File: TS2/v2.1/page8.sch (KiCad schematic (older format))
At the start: 9 parts, among them SW4 ABORT, U28 74LS148, U32 74LS138, U33 74LS138, U34 74LS00, U35 74LS74, U4 74LS06, U7 74LS08

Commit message: Rev 2.1 design changes.
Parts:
- added unit 4 of U34
- added U37: 74LS00, symbol 74LS00
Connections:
- net GND: now also U34.7 (GND), U37.7 (GND)
- net VCC: now also U34.14 (VCC), U37.14 (VCC)
- net at U4.13: now also U34.11; no longer U34.8
- new net: U34.8, U37.10, U37.9
- new net: U34.12, U37.8
- new net PERI_VPA*: U34.13
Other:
- moved on the sheet: U4F
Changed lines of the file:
@@
 Sheet 9 9
 Title "TS2 68000 Single Board Computer"
-Date "2017-02-14"
+Date "2017-02-15"
 Rev "2.1"
 Comp "Jeff Tranter"
@@
 NoConn ~ 2750 2300
 $Comp
-L VCC #PWR0106
+L VCC #PWR0110
 U 1 1 584DE8AD
 P 3550 1550
-F 0 "#PWR0106" H 3550 1400 50  0001 C CNN
+F 0 "#PWR0110" H 3550 1400 50  0001 C CNN
 F 1 "VCC" H 3550 1700 50  0000 C CNN
 F 2 "" H 3550 1550 50  0000 C CNN
@@
 $EndComp
 $Comp
-L GND #PWR0107
+L GND #PWR0111
 U 1 1 584DE8EB
 P 3550 2450
-F 0 "#PWR0107" H 3550 2200 50  0001 C CNN
+F 0 "#PWR0111" H 3550 2200 50  0001 C CNN
 F 1 "GND" H 3550 2300 50  0000 C CNN
 F 2 "" H 3550 2450 50  0000 C CNN
@@
 FC2
 $Comp
-L VCC #PWR0108
+L VCC #PWR0112
 U 1 1 584E001A
 P 2650 4200
-F 0 "#PWR0108" H 2650 4050 50  0001 C CNN
+F 0 "#PWR0112" H 2650 4050 50  0001 C CNN
 F 1 "VCC" H 2650 4350 50  0000 C CNN
 F 2 "" H 2650 4200 50  0000 C CNN
@@
 $EndComp
 $Comp
-L GND #PWR0109
+L GND #PWR0113
 U 1 1 584E0034
 P 2650 4500
-F 0 "#PWR0109" H 2650 4250 50  0001 C CNN
+F 0 "#PWR0113" H 2650 4250 50  0001 C CNN
 F 1 "GND" H 2650 4350 50  0000 C CNN
 F 2 "" H 2650 4500 50  0000 C CNN
@@
 $EndComp
 $Comp
-L GND #PWR0110
+L GND #PWR0114
 U 1 1 584E0412
 P 3350 4500
-F 0 "#PWR0110" H 3350 4250 50  0001 C CNN
+F 0 "#PWR0114" H 3350 4250 50  0001 C CNN
 F 1 "GND" H 3350 4350 50  0000 C CNN
 F 2 "" H 3350 4500 50  0000 C CNN
@@
 $EndComp
 $Comp
-L VCC #PWR0111
+L VCC #PWR0115
 U 1 1 584E042C
 P 3350 3600
-F 0 "#PWR0111" H 3350 3450 50  0001 C CNN
+F 0 "#PWR0115" H 3350 3450 50  0001 C CNN
 F 1 "VCC" H 3350 3750 50  0000 C CNN
 F 2 "" H 3350 3600 50  0000 C CNN
@@
 $EndComp
 $Comp
-L GND #PWR0112
+L GND #PWR0116
 U 1 1 584E07F8
 P 5750 4500
-F 0 "#PWR0112" H 5750 4250 50  0001 C CNN
+F 0 "#PWR0116" H 5750 4250 50  0001 C CNN
 F 1 "GND" H 5750 4350 50  0000 C CNN
 F 2 "" H 5750 4500 50  0000 C CNN
@@
 $EndComp
 $Comp
-L VCC #PWR0113
+L VCC #PWR0117
 U 1 1 584E0812
 P 5750 3600
-F 0 "#PWR0113" H 5750 3450 50  0001 C CNN
+F 0 "#PWR0117" H 5750 3450 50  0001 C CNN
 F 1 "VCC" H 5750 3750 50  0000 C CNN
 F 2 "" H 5750 3600 50  0000 C CNN
@@
 AS*
 $Comp
-L VCC #PWR0114
+L VCC #PWR0118
 U 1 1 584E1E8C
 P 5150 4200
-F 0 "#PWR0114" H 5150 4050 50  0001 C CNN
+F 0 "#PWR0118" H 5150 4050 50  0001 C CNN
 F 1 "VCC" H 5150 4350 50  0000 C CNN
 F 2 "" H 5150 4200 50  0000 C CNN
@@
 NoConn ~ 6350 3700
 $Comp
-L GND #PWR0115
+L GND #PWR0119
 U 1 1 584E3D7F
 P 4100 2500
-F 0 "#PWR0115" H 4100 2250 50  0001 C CNN
+F 0 "#PWR0119" H 4100 2250 50  0001 C CNN
 F 1 "GND" H 4100 2350 50  0000 C CNN
 F 2 "" H 4100 2500 50  0000 C CNN
@@
 $EndComp
 $Comp
-L GND #PWR0116
+L GND #PWR0120
 U 1 1 587AA680
 P 800 6350
-F 0 "#PWR0116" H 800 6100 50  0001 C CNN
+F 0 "#PWR0120" H 800 6100 50  0001 C CNN
 F 1 "GND" H 800 6200 50  0000 C CNN
 F 2 "" H 800 6350 50  0000 C CNN
@@
 $EndComp
 $Comp
-L VCC #PWR0117
+L VCC #PWR0121
 U 1 1 587ACBF3
 P 4800 5850
-F 0 "#PWR0117" H 4800 5700 50  0001 C CNN
+F 0 "#PWR0121" H 4800 5700 50  0001 C CNN
 F 1 "VCC" H 4800 6000 50  0000 C CNN
 F 2 "" H 4800 5850 50  0000 C CNN
@@
 L 74LS06 U4
 U 6 1 587B12E8
-P 9850 4050
-F 0 "U4" H 10045 4165 50  0000 C CNN
-F 1 "74LS06" H 10040 3925 50  0000 C CNN
-F 2 "Housings_DIP:DIP-14_W7.62mm" H 9850 4050 50  0001 C CNN
-F 3 "" H 9850 4050 50  0000 C CNN
-	6    9850 4050
-	1    0    0    -1
-$EndComp
-Text GLabel 10550 4050 2    60   Output ~ 0
+P 9550 5600
+F 0 "U4" H 9745 5715 50  0000 C CNN
+F 1 "74LS06" H 9740 5475 50  0000 C CNN
+F 2 "Housings_DIP:DIP-14_W7.62mm" H 9550 5600 50  0001 C CNN
+F 3 "" H 9550 5600 50  0000 C CNN
+	6    9550 5600
+	1    0    0    -1
+$EndComp
+Text GLabel 10000 5600 2    60   Output ~ 0
 VPA*
 NoConn ~ 6350 3800
@@
 Wire Wire Line
 	5850 2300 3950 2300
-Wire Wire Line
-	10300 4050 10550 4050
-Wire Wire Line
-	9300 4050 9400 4050
 Wire Wire Line
 	8100 3800 8100 3950
@@
 $EndComp
 $Comp
-L VCC #PWR0118
+L VCC #PWR0122
 U 1 1 58867427
 P 1300 4450
-F 0 "#PWR0118" H 1300 4300 50  0001 C CNN
+F 0 "#PWR0122" H 1300 4300 50  0001 C CNN
 F 1 "VCC" H 1300 4600 50  0000 C CNN
 F 2 "" H 1300 4450 50  0000 C CNN
@@
 Text GLabel 5400 6750 2    60   Input ~ 0
 IRQ7*
+$Comp
+L 74LS00 U34
+U 4 1 58A651E7
+P 8500 5600
+F 0 "U34" H 8500 5650 50  0000 C CNN
+F 1 "74LS00" H 8500 5500 50  0000 C CNN
+F 2 "" H 8500 5600 50  0000 C CNN
+F 3 "" H 8500 5600 50  0000 C CNN
+	4    8500 5600
+	1    0    0    -1
+$EndComp
+Text GLabel 7600 5700 0    60   Input ~ 0
+PERI_VPA*
+Wire Wire Line
+	7600 5700 7900 5700
+$Comp
+L 74LS00 U37
+U 3 1 58A65894
+P 8500 4900
+F 0 "U37" H 8500 4950 50  0000 C CNN
+F 1 "74LS00" H 8500 4800 50  0000 C CNN
+F 2 "" H 8500 4900 50  0000 C CNN
+F 3 "" H 8500 4900 50  0000 C CNN
+	3    8500 4900
+	-1   0    0    1
+$EndComp
+Wire Wire Line
+	7900 4900 7900 5500
+Wire Wire Line
+	9300 4050 9300 4900
+Wire Wire Line
+	9300 4900 9100 4900
+Wire Wire Line
+	9100 4800 9100 5000
+Connection ~ 9100 4900
 $EndSCHEMATC

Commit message: Import PCB layout.
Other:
- moved on the sheet: U34D, U4F
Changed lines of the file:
@@
 Sheet 9 9
 Title "TS2 68000 Single Board Computer"
-Date "2017-02-15"
+Date "2017-02-17"
 Rev "2.1"
 Comp "Jeff Tranter"
@@
 L 74LS06 U4
 U 6 1 587B12E8
-P 9550 5600
-F 0 "U4" H 9745 5715 50  0000 C CNN
-F 1 "74LS06" H 9740 5475 50  0000 C CNN
-F 2 "Housings_DIP:DIP-14_W7.62mm" H 9550 5600 50  0001 C CNN
-F 3 "" H 9550 5600 50  0000 C CNN
-	6    9550 5600
-	1    0    0    -1
-$EndComp
-Text GLabel 10000 5600 2    60   Output ~ 0
+P 9550 5850
+F 0 "U4" H 9745 5965 50  0000 C CNN
+F 1 "74LS06" H 9740 5725 50  0000 C CNN
+F 2 "Housings_DIP:DIP-14_W7.62mm" H 9550 5850 50  0001 C CNN
+F 3 "" H 9550 5850 50  0000 C CNN
+	6    9550 5850
+	1    0    0    -1
+$EndComp
+Text GLabel 10000 5850 2    60   Output ~ 0
 VPA*
 NoConn ~ 6350 3800
@@
 L 74LS00 U34
 U 4 1 58A651E7
-P 8500 5600
-F 0 "U34" H 8500 5650 50  0000 C CNN
-F 1 "74LS00" H 8500 5500 50  0000 C CNN
-F 2 "" H 8500 5600 50  0000 C CNN
-F 3 "" H 8500 5600 50  0000 C CNN
-	4    8500 5600
-	1    0    0    -1
-$EndComp
-Text GLabel 7600 5700 0    60   Input ~ 0
+P 8500 5850
+F 0 "U34" H 8500 5900 50  0000 C CNN
+F 1 "74LS00" H 8500 5750 50  0000 C CNN
+F 2 "" H 8500 5850 50  0000 C CNN
+F 3 "" H 8500 5850 50  0000 C CNN
+	4    8500 5850
+	1    0    0    -1
+$EndComp
+Text GLabel 7600 5950 0    60   Input ~ 0
 PERI_VPA*
 Wire Wire Line
-	7600 5700 7900 5700
+	7600 5950 7900 5950
 $Comp
 L 74LS00 U37
@@
 $EndComp
 Wire Wire Line
-	7900 4900 7900 5500
+	7900 4900 7900 5750
 Wire Wire Line
 	9300 4050 9300 4900

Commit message: Rev 2.1.1 changes.
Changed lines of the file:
@@
 EELAYER 25 0
 EELAYER END
-$Descr A4 11693 8268
+$Descr A 11000 8500
 encoding utf-8
 Sheet 9 9
 Title "TS2 68000 Single Board Computer"
-Date "2017-02-17"
-Rev "2.1"
+Date "2017-05-29"
+Rev "2.1.1"
 Comp "Jeff Tranter"
 Comment1 "Interrupt Control Circuitry (optional)"
@@
 Text GLabel 1300 5050 2    60   Input ~ 0
 IRQ6*
-Text GLabel 5400 6750 2    60   Input ~ 0
+Text GLabel 5400 6750 2    60   Output ~ 0
 IRQ7*
 $Comp

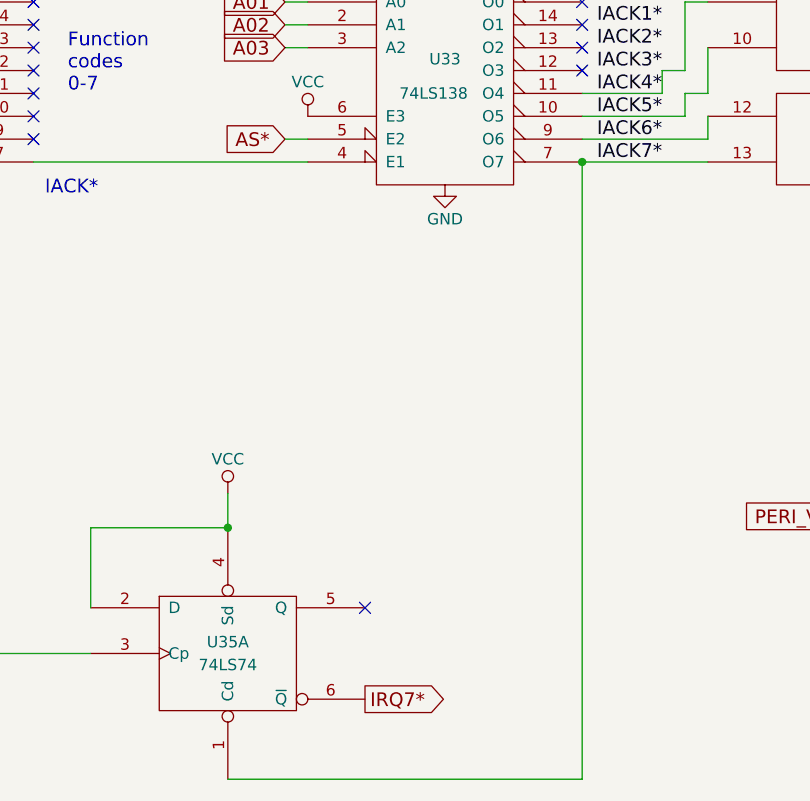
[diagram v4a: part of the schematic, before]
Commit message: Check in rev 2.1.1 PCB layout.
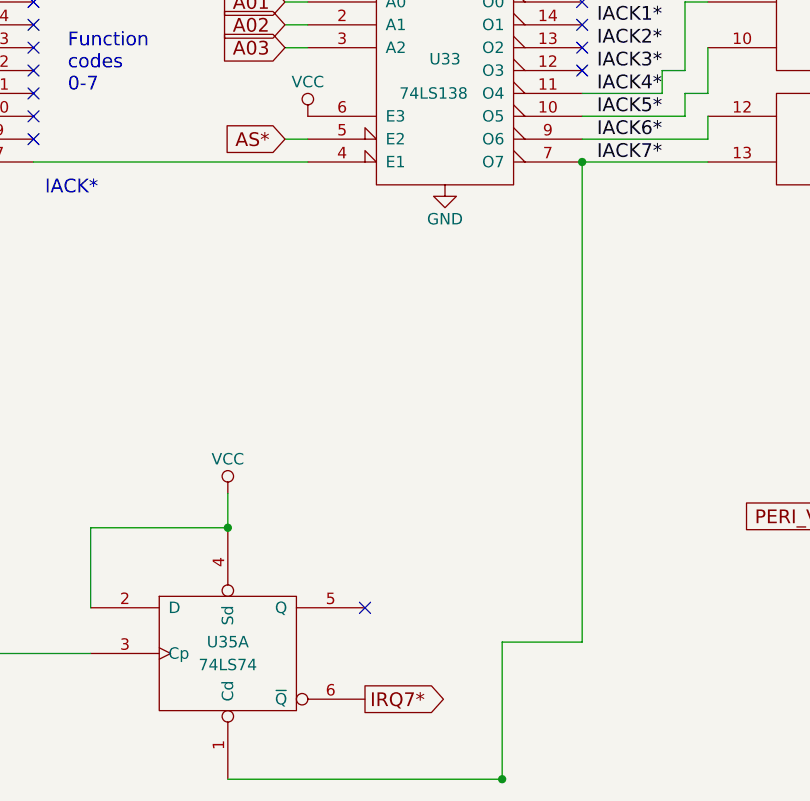
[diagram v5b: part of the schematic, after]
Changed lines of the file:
@@
 	4200 6000 4200 6350
 Connection ~ 4800 6000
-Wire Wire Line
-	6350 7100 6350 4400
 Connection ~ 6350 4400
-Wire Wire Line
-	4800 7100 6350 7100
 Wire Wire Line
 	3950 4400 5150 4400
@@
 	9100 4800 9100 5000
 Connection ~ 9100 4900
+Wire Wire Line
+	6000 7100 6000 6500
+Wire Wire Line
+	6000 6500 6350 6500
+Wire Wire Line
+	6350 6500 6350 4400
+Connection ~ 6000 7100
+Wire Wire Line
+	4800 7100 6000 7100
 $EndSCHEMATC
